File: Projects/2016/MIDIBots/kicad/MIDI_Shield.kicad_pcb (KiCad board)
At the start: 2 copper layers, 69 parts, among them IC1 PC900V, K1 SRVO1, K2 SRVO2, K3 SRVO3, P10 A3, P11 A4, P12 AUX_12V, P13 AUX_12V, P14 AUX_5V, P15 AUX_5V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

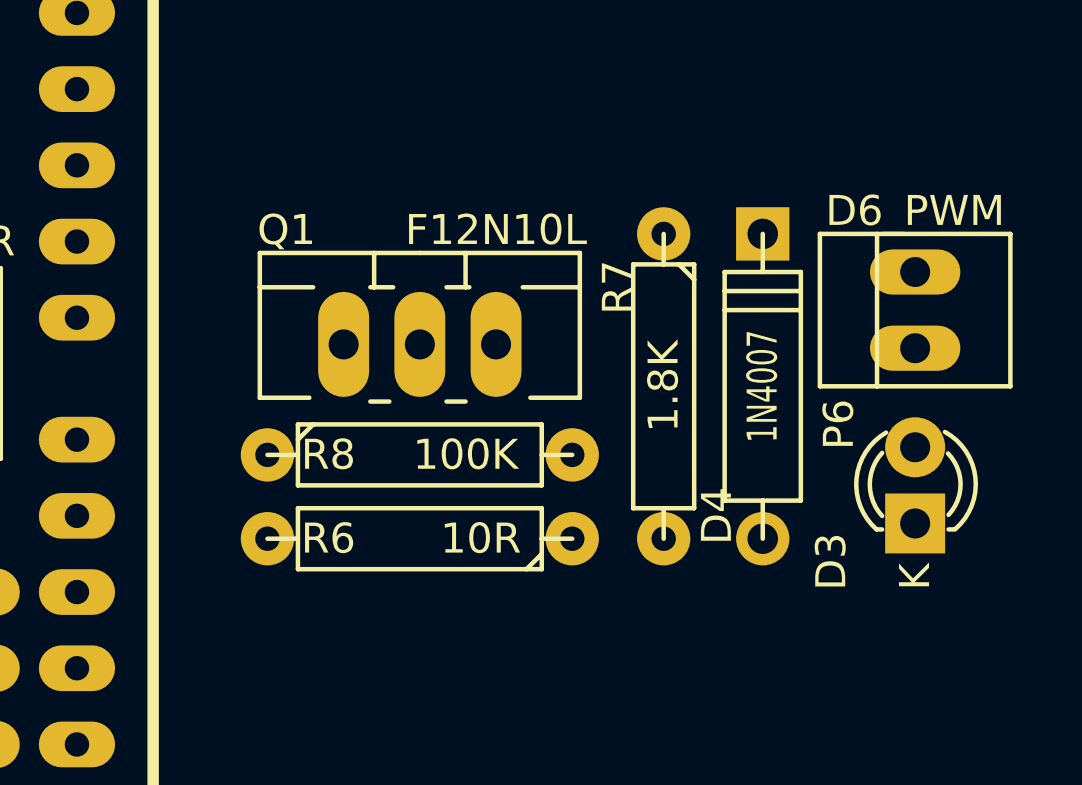
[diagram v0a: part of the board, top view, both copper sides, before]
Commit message: Added alignment targets to the 10x10 cm corners
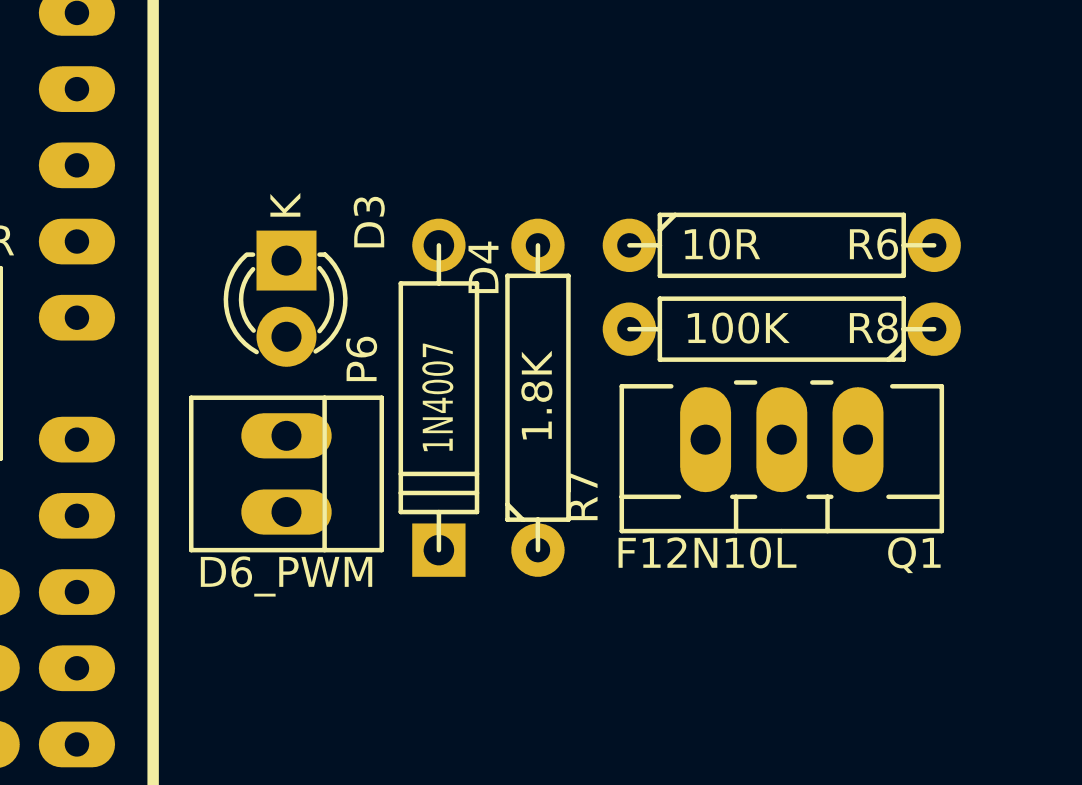
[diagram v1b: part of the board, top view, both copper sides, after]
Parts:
- moved D3 22.7 mm to (128.9, 121.0), turned to 270 degrees
- moved P6 21.7 mm to (128.9, 128.1), turned to 270 degrees
- moved R6 15.5 mm to (145.4, 120.5), turned to 0 degrees
- moved R8 12.8 mm to (145.4, 123.3), turned to 180 degrees
- moved Q1 12.5 mm to (145.4, 127.0), turned to 180 degrees
- moved D4 10.8 mm to (134.0, 125.6), turned to 270 degrees
- moved R7 4.21 mm to (137.3, 125.6), turned to 90 degrees

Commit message: Physical part placement basically ready for routing now, I think...
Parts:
- moved D13 34.9 mm to (66.0, 143.5), turned to 0 degrees
- moved P11 33.3 mm to (60.3, 143.5), turned to 180 degrees
- moved D11 31.9 mm to (66.0, 113.7), turned to 0 degrees
- moved P12 31.2 mm to (92.3, 108.3)
- moved P13 31.2 mm to (92.3, 103.3)
- moved P14 31.2 mm to (98.7, 103.3)
- moved P15 31.2 mm to (98.7, 108.3)
- moved R10 31.2 mm to (106.0, 99.4)
- moved R9 31.2 mm to (84.7, 99.4)
- moved C4 31.2 mm to (88.3, 92.1)
- moved C5 31.2 mm to (89.3, 86.2)
- moved C6 31.2 mm to (101.5, 86.2)
- moved C7 31.2 mm to (102.2, 92.1)
- moved D10 31.2 mm to (106.0, 87.0)
- moved D9 31.2 mm to (84.7, 87.0)
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
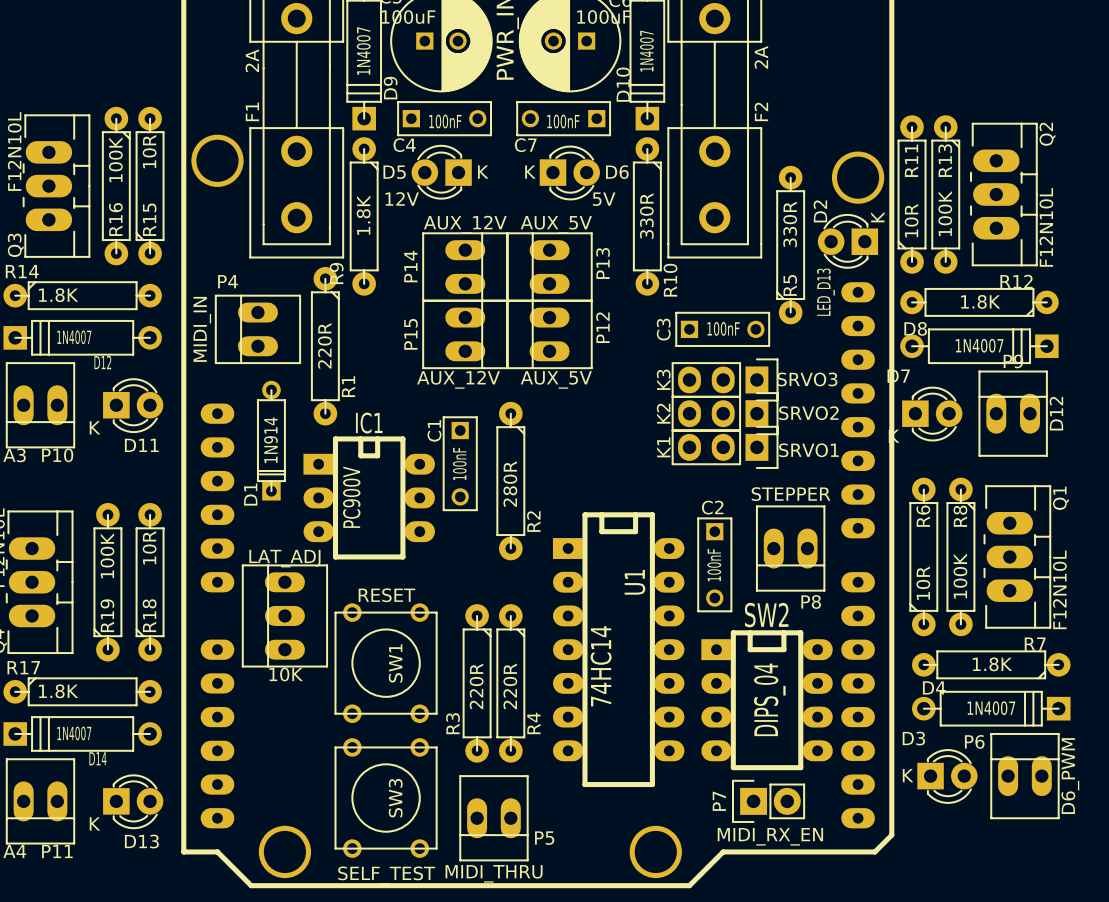
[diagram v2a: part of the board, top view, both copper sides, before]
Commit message: [Y] Move LAT_ADJ label so it won't be covered by the PC900V IC socket [Y] Move the servo headers to the left a little [Y] Label SW2 as CH or MIDI_CH [Y] Correct layout orientation of input diode D1 [Y] Move some part reference labels to be visible
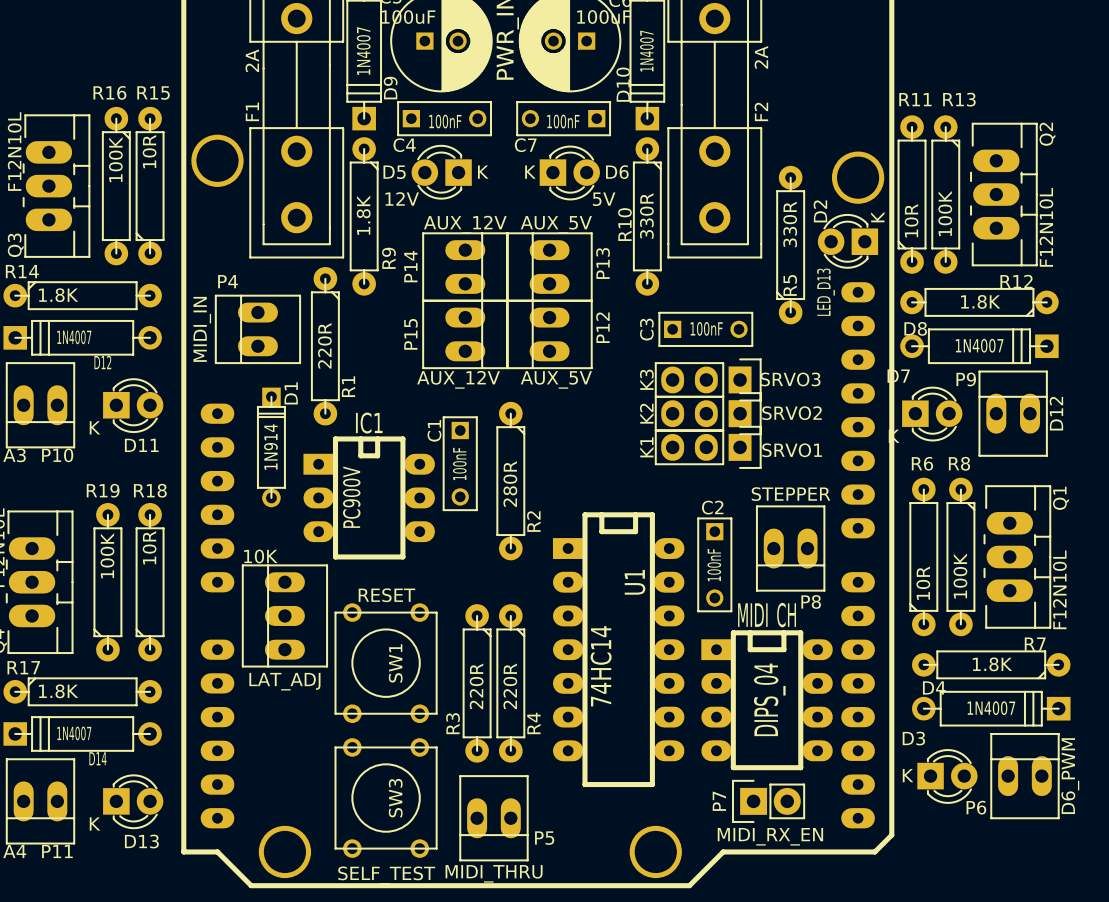
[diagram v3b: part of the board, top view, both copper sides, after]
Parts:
- moved C3 1.27 mm to (108.0, 108.0)
- moved K1 1.27 mm to (113.0, 116.8)
- moved K2 1.27 mm to (113.0, 114.3)
- moved K3 1.27 mm to (113.0, 111.8)
- moved D1 0.51 mm to (77.7, 116.8), turned to 90 degrees
- renumbered SW2 to MIDI_CH
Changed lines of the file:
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@@
     (descr "8 pins DIL package, elliptical pads")
     (tags DIL)
-    (fp_text reference SW2 (at -6.35 0 360) (layer F.SilkS)
-      (effects (font (size 1.778 1.143) (thickness 0.3048)))
+    (fp_text reference MIDI_CH (at -6.35 0 360) (layer F.SilkS)
+      (effects (font (size 1.778 0.8) (thickness 0.15)))
     )
     (fp_text value DIPS_04 (at 0 0 270) (layer F.SilkS)
@@
   )
   (module Capacitors_ThroughHole:C_Rect_L7_W2.5_P5 (layer F.Cu)
-    (at 109.22 107.95)
+    (at 107.95 107.95)
     (descr "Film Capacitor Length 7mm x Width 2.5mm, Pitch 5mm")
     (tags Capacitor)
@@
   )
   (module Pin_Headers:Pin_Header_Straight_1x03 (layer F.Cu)
-    (at 114.3 116.84 270)
+    (at 113.03 116.84 270)
     (descr "Through hole pin header")
     (tags "pin header")
@@
   )
   (module Pin_Headers:Pin_Header_Straight_1x03 (layer F.Cu)
-    (at 114.3 114.3 270)
+    (at 113.03 114.3 270)
     (descr "Through hole pin header")
     (tags "pin header")
@@
   )
   (module Pin_Headers:Pin_Header_Straight_1x03 (layer F.Cu)
-    (at 114.3 111.76 270)
+    (at 113.03 111.76 270)
     (descr "Through hole pin header")
     (tags "pin header")
@@
     (at 134.493 141.605)
     (attr virtual)
-    (fp_text reference P6 (at -3.81 -2.54) (layer F.SilkS)
+    (fp_text reference P6 (at -3.683 2.413) (layer F.SilkS)
       (effects (font (size 1 1) (thickness 0.15)))
     )
@@
     (at 133.604 114.3)
     (attr virtual)
-    (fp_text reference P9 (at 0 -3.9) (layer F.SilkS)
+    (fp_text reference P9 (at -3.556 -2.54) (layer F.SilkS)
       (effects (font (size 1 1) (thickness 0.15)))
     )
@@
     (at 78.74 129.54 90)
     (attr virtual)
-    (fp_text reference LAT_ADJ (at 4.445 0 180) (layer F.SilkS)
-      (effects (font (size 1 1) (thickness 0.15)))
-    )
-    (fp_text value 10K (at -4.445 0 180) (layer F.SilkS)
+    (fp_text reference LAT_ADJ (at -4.826 0 180) (layer F.SilkS)
+      (effects (font (size 1 1) (thickness 0.15)))
+    )
+    (fp_text value 10K (at 4.445 -1.905 180) (layer F.SilkS)
       (effects (font (size 1 1) (thickness 0.15)))
     )
@@
   )
   (module Discret:D3 (layer F.Cu)
-    (at 77.724 116.332 270)
+    (at 77.724 116.84 90)
     (descr "Diode 3 pas")
     (tags "DIODE DEV")
-    (fp_text reference D1 (at 4.064 1.524 270) (layer F.SilkS)
-      (effects (font (size 1 1) (thickness 0.15)))
-    )
-    (fp_text value 1N914 (at 0 0 270) (layer F.SilkS)
+    (fp_text reference D1 (at 4.064 1.524 90) (layer F.SilkS)
+      (effects (font (size 1 1) (thickness 0.15)))
+    )
+    (fp_text value 1N914 (at 0 0 90) (layer F.SilkS)
       (effects (font (size 1 0.8) (thickness 0.15)))
     )
@@
     (fp_line (start 2.54 -1.016) (end 2.54 1.016) (layer F.SilkS) (width 0.15))
     (fp_line (start 2.286 1.016) (end 2.286 -1.016) (layer F.SilkS) (width 0.15))
-    (pad 1 thru_hole rect (at 3.81 0 270) (size 1.397 1.397) (drill 0.8128) (layers *.Cu *.Mask F.SilkS)
+    (pad 1 thru_hole rect (at 3.81 0 90) (size 1.397 1.397) (drill 0.8128) (layers *.Cu *.Mask F.SilkS)
       (net 33 "Net-(D1-Pad1)"))
-    (pad 2 thru_hole circle (at -3.81 0 270) (size 1.397 1.397) (drill 0.8128) (layers *.Cu *.Mask F.SilkS)
+    (pad 2 thru_hole circle (at -3.81 0 90) (size 1.397 1.397) (drill 0.8128) (layers *.Cu *.Mask F.SilkS)
       (net 34 "Net-(D1-Pad2)"))
     (model Discret.3dshapes/D3.wrl
@@
     (descr "Resitance 4 pas")
     (tags R)
-    (fp_text reference R15 (at -2.54 0 90) (layer F.SilkS)
+    (fp_text reference R15 (at 6.985 0.254 180) (layer F.SilkS)
       (effects (font (size 1 1) (thickness 0.15)))
     )
@@
     (descr "Resitance 4 pas")
     (tags R)
-    (fp_text reference R16 (at 2.54 0 270) (layer F.SilkS)
+    (fp_text reference R16 (at -6.985 0.508 360) (layer F.SilkS)
       (effects (font (size 1 1) (thickness 0.15)))
     )
@@
     (descr "Resitance 4 pas")
     (tags R)
-    (fp_text reference R18 (at -2.54 0 90) (layer F.SilkS)
+    (fp_text reference R18 (at 6.858 0 180) (layer F.SilkS)
       (effects (font (size 1 1) (thickness 0.15)))
     )
@@
     (descr "Resitance 4 pas")
     (tags R)
-    (fp_text reference R19 (at -2.54 0 90) (layer F.SilkS)
+    (fp_text reference R19 (at 6.858 -0.381 180) (layer F.SilkS)
       (effects (font (size 1 1) (thickness 0.15)))
     )
@@
     (descr "Resitance 4 pas")
     (tags R)
-    (fp_text reference R6 (at 3.048 0 90) (layer F.SilkS)
+    (fp_text reference R6 (at 6.985 -0.127 180) (layer F.SilkS)
       (effects (font (size 1 1) (thickness 0.15)))
     )
@@
     (descr "Resitance 4 pas")
     (tags R)
-    (fp_text reference R8 (at -3.048 0 270) (layer F.SilkS)
+    (fp_text reference R8 (at -6.985 0.127 360) (layer F.SilkS)
       (effects (font (size 1 1) (thickness 0.15)))
     )
@@
     (descr "Resitance 4 pas")
     (tags R)
-    (fp_text reference R9 (at 4.318 2.032 270) (layer F.SilkS)
+    (fp_text reference R9 (at 3.175 -1.905 270) (layer F.SilkS)
       (effects (font (size 1 1) (thickness 0.15)))
     )
@@
     (descr "Resitance 4 pas")
     (tags R)
-    (fp_text reference R10 (at 4.826 -1.778 270) (layer F.SilkS)
+    (fp_text reference R10 (at 0.635 1.651 270) (layer F.SilkS)
       (effects (font (size 1 1) (thickness 0.15)))
     )
@@
     (descr "Resitance 4 pas")
     (tags R)
-    (fp_text reference R11 (at 2.54 0 90) (layer F.SilkS)
+    (fp_text reference R11 (at 7.112 0.254 180) (layer F.SilkS)
       (effects (font (size 1 1) (thickness 0.15)))
     )
@@
     (descr "Resitance 4 pas")
     (tags R)
-    (fp_text reference R13 (at -2.54 0 270) (layer F.SilkS)
-      (effects (font (size 1 1) (thickness 0.15)))
-    )
+    (fp_text reference R13 (at -7.112 -1.016 360) (layer F.SilkS)
+      (effects (font (size 1 1) (thickness 0.15)))
+    )

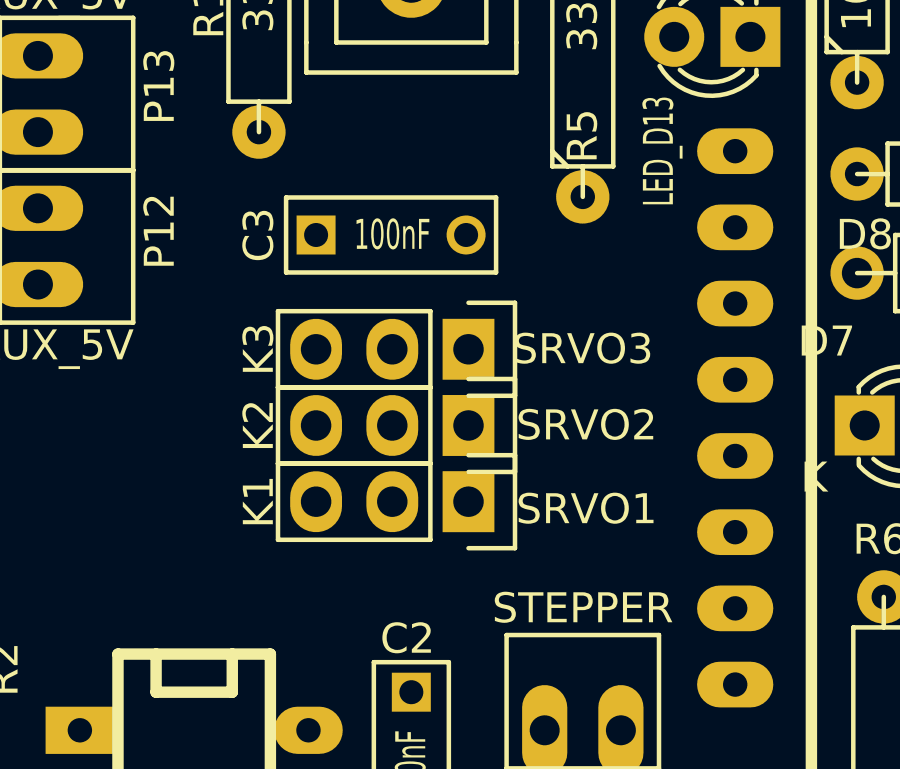
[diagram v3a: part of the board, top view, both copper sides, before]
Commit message: Spaced servo headers out to allow control tracks to be routed
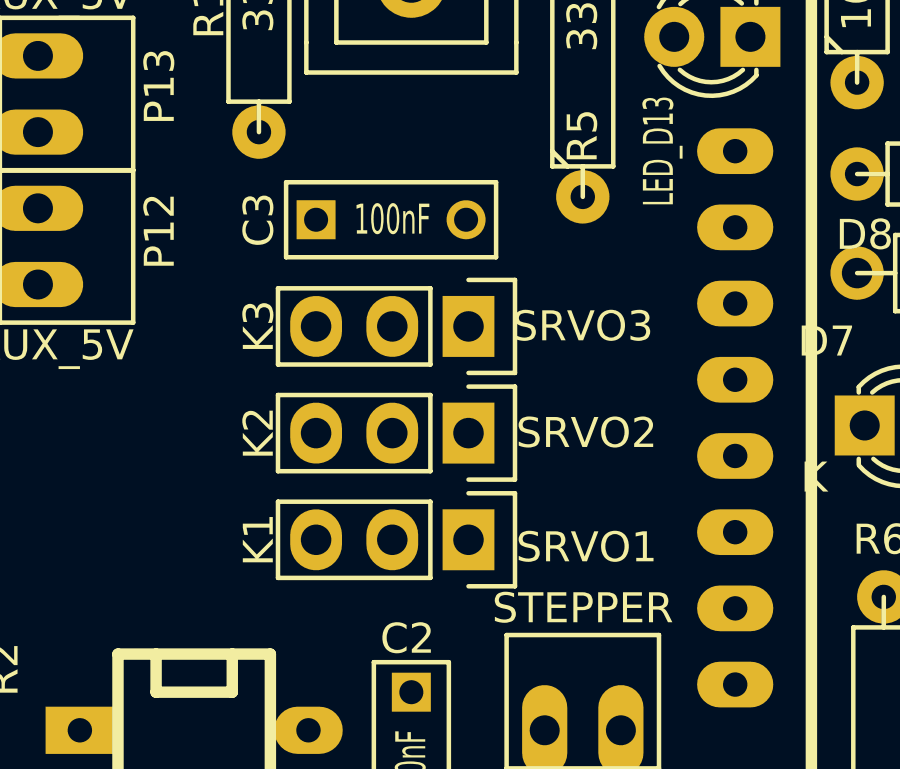
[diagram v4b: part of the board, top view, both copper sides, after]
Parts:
- moved K1 1.27 mm to (113.0, 118.1)
- moved K3 0.76 mm to (113.0, 111.0)
- moved C3 0.51 mm to (108.0, 107.4)
- moved K2 0.25 mm to (113.0, 114.6)
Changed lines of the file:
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@@
   )
   (module Capacitors_ThroughHole:C_Rect_L7_W2.5_P5 (layer F.Cu)
-    (at 107.95 107.95)
+    (at 107.95 107.442)
     (descr "Film Capacitor Length 7mm x Width 2.5mm, Pitch 5mm")
     (tags Capacitor)
@@
   )
   (module Pin_Headers:Pin_Header_Straight_1x03 (layer F.Cu)
-    (at 113.03 116.84 270)
+    (at 113.03 118.11 270)
     (descr "Through hole pin header")
     (tags "pin header")
@@
   )
   (module Pin_Headers:Pin_Header_Straight_1x03 (layer F.Cu)
-    (at 113.03 114.3 270)
+    (at 113.03 114.554 270)
     (descr "Through hole pin header")
     (tags "pin header")
@@
   )
   (module Pin_Headers:Pin_Header_Straight_1x03 (layer F.Cu)
-    (at 113.03 111.76 270)
+    (at 113.03 110.998 270)
     (descr "Through hole pin header")
     (tags "pin header")
